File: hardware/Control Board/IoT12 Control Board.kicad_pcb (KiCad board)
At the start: 2 copper layers, 99.1 x 69.8 mm, 122 parts, among them J10 USB_B_Micro, J11 Conn_ARM_JTAG_SWD_10, J9 Conn_ARM_JTAG_SWD_10, Q1 MMBT2222, Q2 MMBT2222, Q3 AOD403, SW1 Rotary encoder EC11 Plum 15mm, SW2 SW_Push, U1 ATSAMD21G18A-AU, U2 ADS1115IDGS, U3 INA826AID, U4 INA826AID, U5 LM2596S-ADJ, U6 AT24C32, U7 MAX809S, Y1 32768Hz

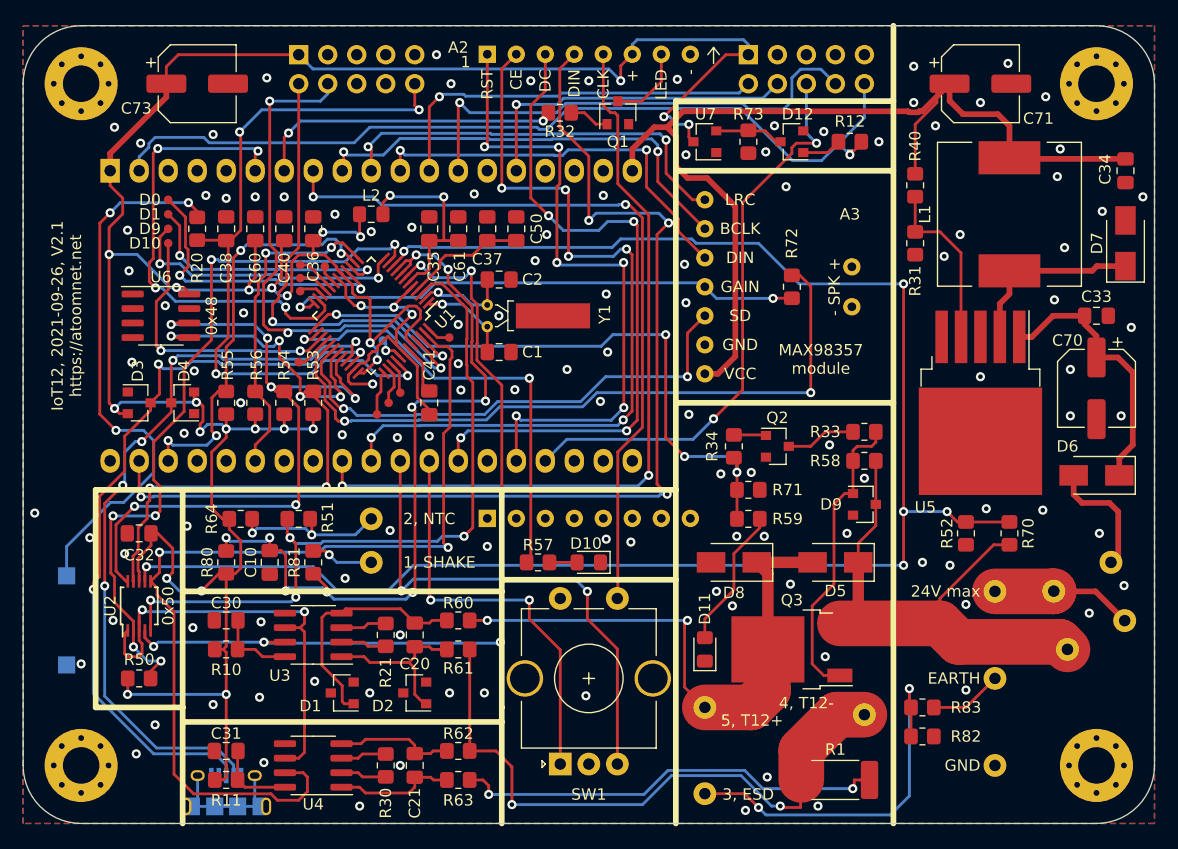
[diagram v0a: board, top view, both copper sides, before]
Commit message: Kicad 5 to 6 upgrade.
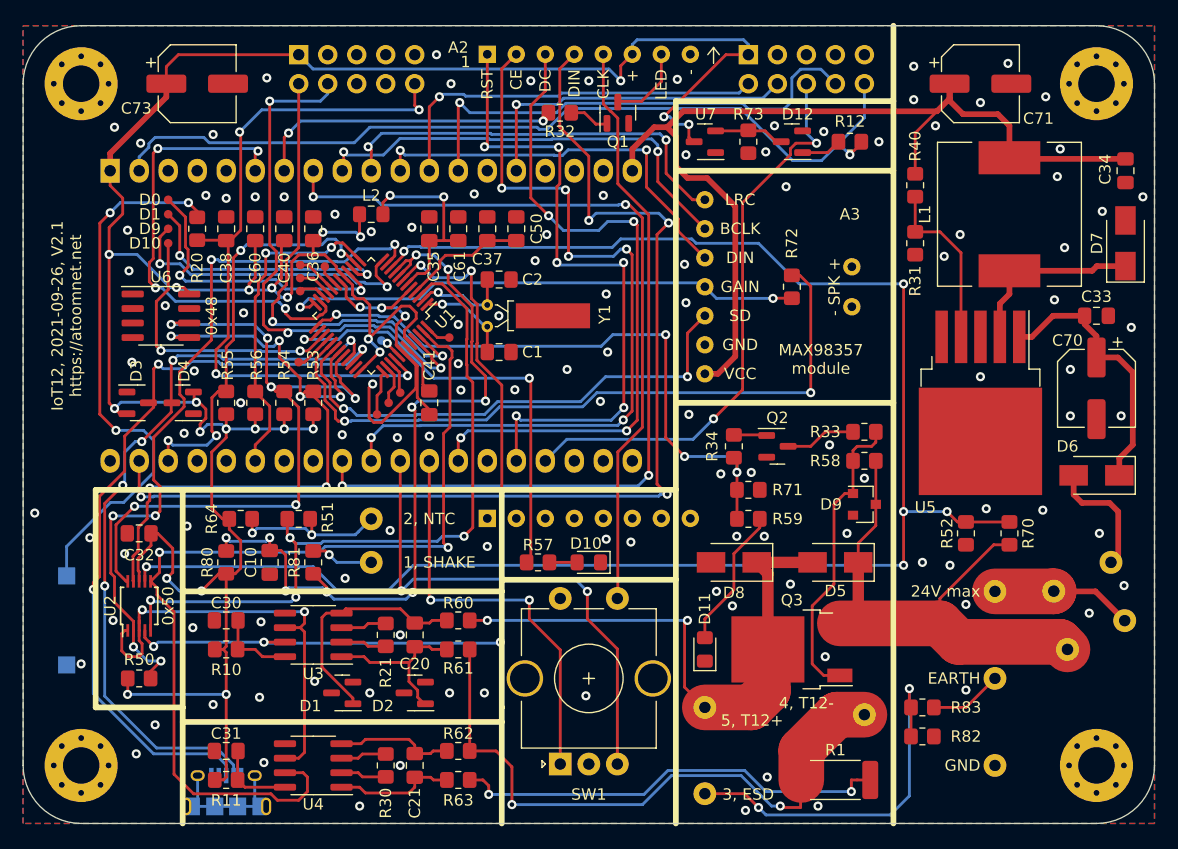
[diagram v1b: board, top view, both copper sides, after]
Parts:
- R1: footprint Resistor_SMD:R_2512_6332Metric_Pad1.52x3.35mm_HandSolder -> Resistor_SMD:R_2512_6332Metric_Pad1.40x3.35mm_HandSolder
- moved NT5 0.25 mm to (23.2, 24.1)
- moved D3 0.13 mm to (-39.5, -8.89)
- moved TP14 0.13 mm to (-18.2, -14.4)
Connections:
- net ESP32_~RESET renamed ESP32_~{RESET}
- net HEAT_~RESET renamed HEAT_~{RESET}
- net LCD_DATA-~CMD renamed LCD_DATA-~{CMD}
- net LCD_~CE renamed LCD_~{CE}
- net LCD_~RST renamed LCD_~{RST}
- A1 pad 16: Net-(A1-Pad16) -> unconnected-(A1-Pad16)
- A1 pad 17: Net-(A1-Pad17) -> unconnected-(A1-Pad17)
- A1 pad 18: Net-(A1-Pad18) -> unconnected-(A1-Pad18)
- A1 pad 20: Net-(A1-Pad20) -> unconnected-(A1-Pad20)
- A1 pad 21: Net-(A1-Pad21) -> unconnected-(A1-Pad21)
- A1 pad 22: Net-(A1-Pad22) -> unconnected-(A1-Pad22)
- A1 pad 25: Net-(A1-Pad25) -> unconnected-(A1-Pad25)
- A1 pad 3: Net-(A1-Pad3) -> unconnected-(A1-Pad3)
- A1 pad 31: Net-(A1-Pad31) -> unconnected-(A1-Pad31)
- A1 pad 34: Net-(A1-Pad34) -> unconnected-(A1-Pad34)
- A1 pad 35: Net-(A1-Pad35) -> unconnected-(A1-Pad35)
- A1 pad 4: Net-(A1-Pad4) -> unconnected-(A1-Pad4)
- A1 pad 5: Net-(A1-Pad5) -> unconnected-(A1-Pad5)
- A3 pad 8: Net-(A3-Pad8) -> unconnected-(A3-Pad8)
- A3 pad 9: Net-(A3-Pad9) -> unconnected-(A3-Pad9)
- D12 pad 2: Net-(D12-Pad2) -> unconnected-(D12-Pad2)
- J10 pad 1: Net-(J10-Pad1) -> unconnected-(J10-Pad1)
- J10 pad 4: Net-(J10-Pad4) -> unconnected-(J10-Pad4)
- J10 pad 6: Net-(J10-Pad6) -> unconnected-(J10-Pad6)
- J11 pad 6: Net-(J11-Pad6) -> unconnected-(J11-Pad6)
- J11 pad 7: Net-(J11-Pad7) -> unconnected-(J11-Pad7)
- J11 pad 8: Net-(J11-Pad8) -> unconnected-(J11-Pad8)
- J9 pad 7: Net-(J9-Pad7) -> unconnected-(J9-Pad7)
- U6 pad 1: Net-(U6-Pad1) -> unconnected-(U6-Pad1)
- U6 pad 2: Net-(U6-Pad2) -> unconnected-(U6-Pad2)
- U6 pad 3: Net-(U6-Pad3) -> unconnected-(U6-Pad3)
- U6 pad 7: Net-(U6-Pad7) -> unconnected-(U6-Pad7)
- Y1 pad 3: Net-(Y1-Pad3) -> unconnected-(Y1-Pad3)
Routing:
- net Net-(J10-Pad6): track 11.9 -> 0.00 mm
- net unconnected-(J10-Pad6): track 0.00 -> 11.5 mm
- net GND: track 39.4 -> 42.5 mm
- net /Brain/D9: track 25.0 -> 27.3 mm
- net +5V: track 88.3 -> 89.5 mm
- net HEAT_~{RESET}: track 63.5 -> 62.5 mm
- net +3V3: track 259.0 -> 258.3 mm
- net /Brain/USB+: track 66.6 -> 67.1 mm
- net Net-(C20-Pad1): track 21.0 -> 20.5 mm
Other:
- net class Default removed
